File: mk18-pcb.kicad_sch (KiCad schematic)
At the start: 77 parts, among them J10 Conn_02x07_Top_Bottom, J17 Conn_01x06_Socket, J18 Conn_01x06_Socket, J19 Conn_01x06_Socket, J20 Conn_01x06_Socket, J7 Conn_02x06_Top_Bottom, J8 Conn_02x07_Top_Bottom, J9 Conn_02x06_Top_Bottom, P1 FH26W-13S-0_3SHW(60), P10 FH26W-13S-0_3SHW(60), P11 FH26W-13S-0_3SHW(60), P2 FH26W-13S-0_3SHW(60), P3 FH26W-13S-0_3SHW(60), P4 FH26W-13S-0_3SHW(60), P5 FH26W-13S-0_3SHW(60), P6 FH26W-13S-0_3SHW(60), P7 FH26W-13S-0_3SHW(60), P8 FH26W-13S-0_3SHW(60), P9 FH26W-13S-0_3SHW(60), U1 TYPE-C-31-M-12, U10 1N4148W_C81598, U11 1N4148W_C81598, U12 1N4148W_C81598, U13 1N4148W_C81598, U14 1N4148W_C81598, U15 1N4148W_C81598, U16 ECT818001569, U17 HC-FPC-05-10-16RLTAG, U2 AZC199-04S-MS, U4 SN74LVC1T45DRL, U9 1N4148W_C81598

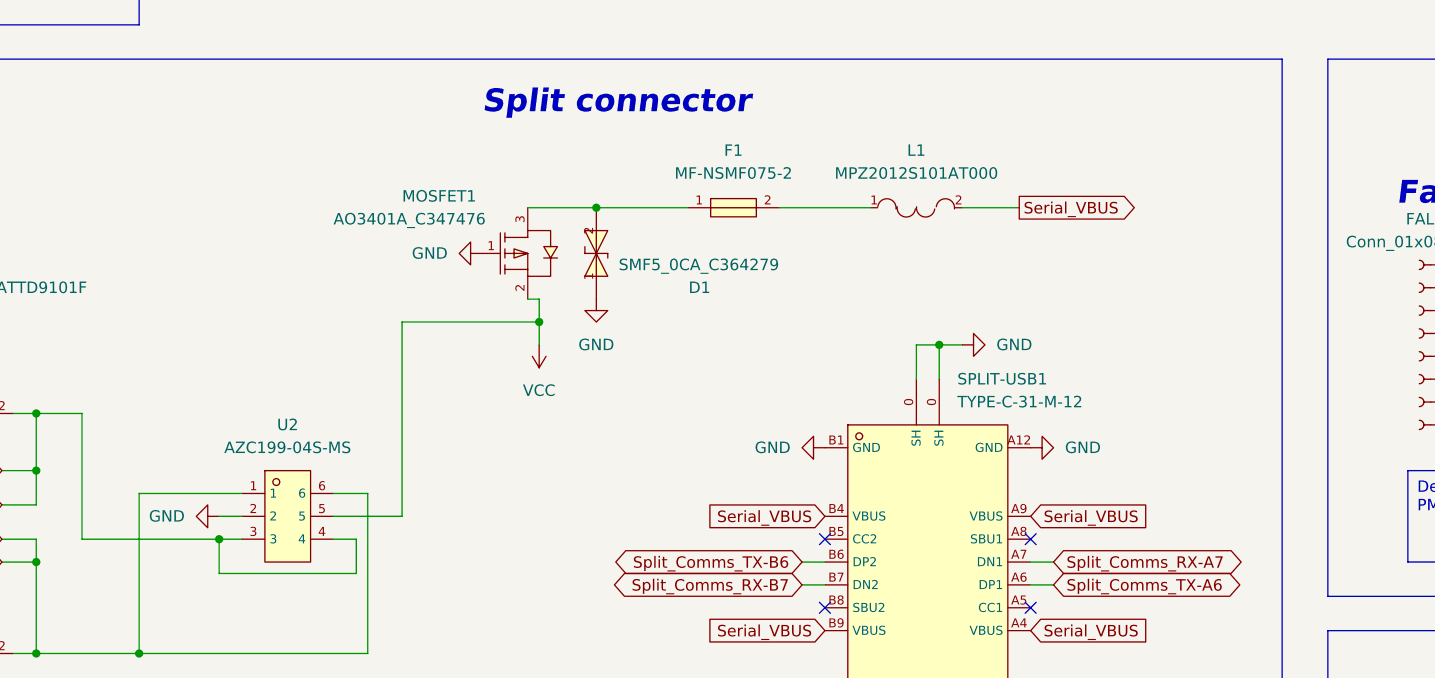
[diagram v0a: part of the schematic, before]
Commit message: added bypass for safeties
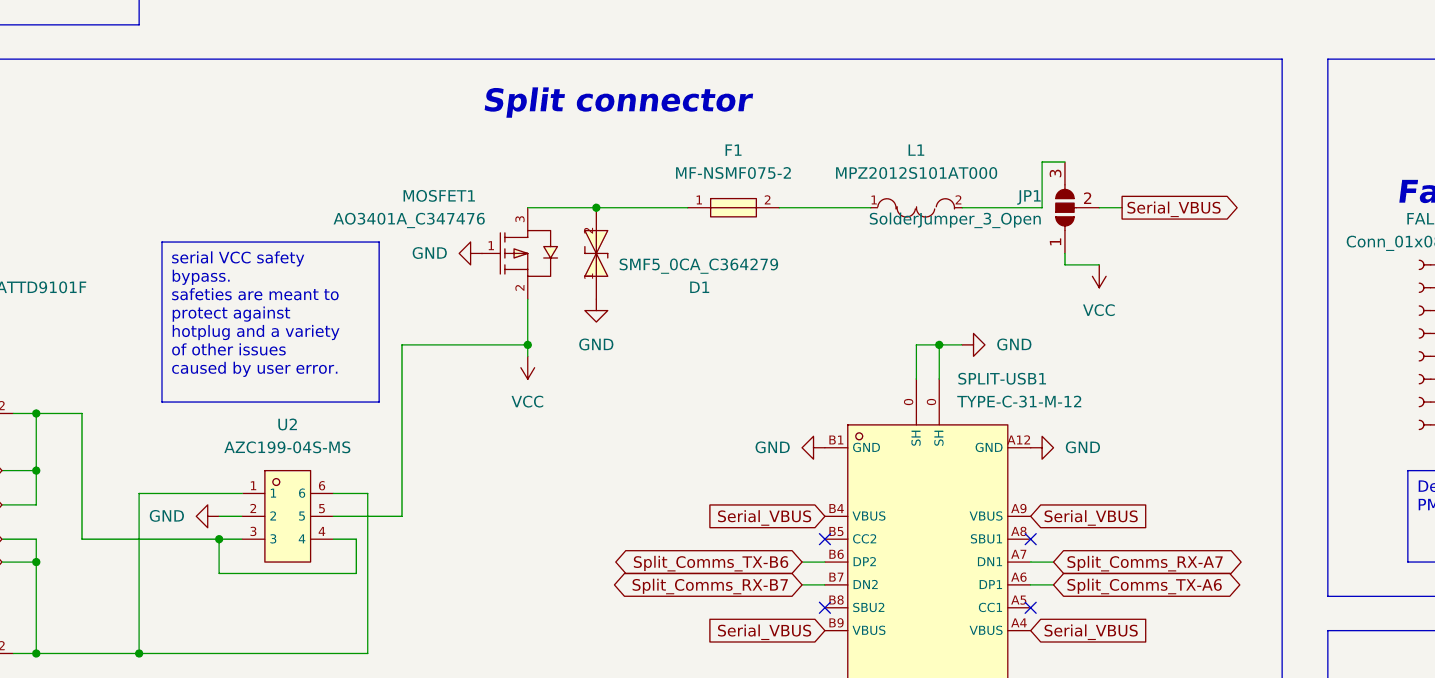
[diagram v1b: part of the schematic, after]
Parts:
- added JP1: SolderJumper_3_Open, Jumper:SolderJumper-3_P1.3mm_Open_RoundedPad1.0x1.5mm, symbol Jumper:SolderJumper_3_Open
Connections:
- net Serial_VBUS: now also JP1.2 (C); no longer L1.2
- net VCC: now also JP1.1 (A)
- new net: JP1.3 (B), L1.2
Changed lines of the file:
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@@
   (junction (at 361.95 284.48) (diameter 0) (color 0 0 0 0)
   )
-  (junction (at 111.76 92.71) (diameter 0) (color 0 0 0 0)
-  )
   (junction (at 232.41 149.86) (diameter 0) (color 0 0 0 0)
   )
@@
   (junction (at 67.31 129.54) (diameter 0) (color 0 0 0 0)
   )
+  (junction (at 110.49 95.25) (diameter 0) (color 0 0 0 0)
+  )
   (junction (at 400.05 185.42) (diameter 0) (color 0 0 0 0)
   )
@@
     (stroke (width 0) (type default))
   )
+  (wire (pts (xy 96.52 95.25) (xy 96.52 114.3))
+    (stroke (width 0) (type default))
+  )
   (wire (pts (xy 295.91 212.09) (xy 295.91 213.36))
     (stroke (width 0) (type default))
@@
     (stroke (width 0) (type default))
   )
-  (wire (pts (xy 111.76 92.71) (xy 111.76 95.25))
-    (stroke (width 0) (type default))
-  )
   (wire (pts (xy 276.86 203.2) (xy 279.4 203.2))
     (stroke (width 0) (type default))
@@
     (stroke (width 0) (type default))
   )
+  (wire (pts (xy 170.18 85.09) (xy 170.18 86.36))
+    (stroke (width 0) (type default))
+  )
   (wire (pts (xy 266.7 276.86) (xy 270.51 276.86))
     (stroke (width 0) (type default))
@@
     (stroke (width 0) (type default))
   )
-  (wire (pts (xy 110.49 90.17) (xy 111.76 90.17))
-    (stroke (width 0) (type default))
-  )
   (wire (pts (xy 214.63 93.98) (xy 224.79 93.98))
     (stroke (width 0) (type default))
@@
     (stroke (width 0) (type default))
   )
-  (wire (pts (xy 111.76 90.17) (xy 111.76 92.71))
-    (stroke (width 0) (type default))
-  )
   (wire (pts (xy 232.41 157.48) (xy 236.22 157.48))
     (stroke (width 0) (type default))
@@
     (stroke (width 0) (type default))
   )
-  (wire (pts (xy 158.75 80.01) (xy 165.1 80.01))
-    (stroke (width 0) (type default))
-  )
   (wire (pts (xy 610.87 280.67) (xy 610.87 292.1))
     (stroke (width 0) (type default))
@@
     (stroke (width 0) (type default))
   )
+  (wire (pts (xy 170.18 86.36) (xy 173.99 86.36))
+    (stroke (width 0) (type default))
+  )
   (wire (pts (xy 359.41 275.59) (xy 359.41 280.67))
     (stroke (width 0) (type default))
@@
     (stroke (width 0) (type default))
   )
+  (wire (pts (xy 173.99 80.01) (xy 176.53 80.01))
+    (stroke (width 0) (type default))
+  )
   (wire (pts (xy 459.74 254) (xy 457.2 254))
     (stroke (width 0) (type default))
@@
     (stroke (width 0) (type default))
   )
+  (wire (pts (xy 110.49 95.25) (xy 110.49 96.52))
+    (stroke (width 0) (type default))
+  )
   (wire (pts (xy 619.76 220.98) (xy 619.76 223.52))
     (stroke (width 0) (type default))
@@
     (stroke (width 0) (type default))
   )
+  (wire (pts (xy 96.52 95.25) (xy 110.49 95.25))
+    (stroke (width 0) (type default))
+  )
   (wire (pts (xy 312.42 379.73) (xy 321.31 379.73))
     (stroke (width 0) (type default))
@@
     (stroke (width 0) (type default))
   )
+  (wire (pts (xy 167.64 74.93) (xy 170.18 74.93))
+    (stroke (width 0) (type default))
+  )
   (wire (pts (xy 71.12 210.82) (xy 93.98 210.82))
     (stroke (width 0) (type default))
@@
     (stroke (width 0) (type default))
   )
+  (wire (pts (xy 167.64 80.01) (xy 167.64 74.93))
+    (stroke (width 0) (type default))
+  )
   (wire (pts (xy 38.1 391.16) (xy 40.64 391.16))
     (stroke (width 0) (type default))
@@
     (stroke (width 0) (type default))
   )
-  (wire (pts (xy 111.76 92.71) (xy 96.52 92.71))
-    (stroke (width 0) (type default))
-  )
   (wire (pts (xy 365.76 368.3) (xy 368.3 368.3))
     (stroke (width 0) (type default))
@@
     (stroke (width 0) (type default))
   )
-  (wire (pts (xy 96.52 92.71) (xy 96.52 114.3))
-    (stroke (width 0) (type default))
-  )
   (wire (pts (xy 401.32 217.17) (xy 403.86 217.17))
     (stroke (width 0) (type default))
@@
     (stroke (width 0) (type default))
   )
+  (wire (pts (xy 110.49 90.17) (xy 110.49 95.25))
+    (stroke (width 0) (type default))
+  )
   (wire (pts (xy 234.95 382.27) (xy 234.95 386.08))
     (stroke (width 0) (type default))
@@
     (stroke (width 0) (type default))
   )
+  (wire (pts (xy 158.75 80.01) (xy 167.64 80.01))
+    (stroke (width 0) (type default))
+  )
   (wire (pts (xy 492.76 403.86) (xy 495.3 403.86))
     (stroke (width 0) (type default))
@@
     (effects (font (size 1.27 1.27)) (justify left top))
   )
+  (text_box "serial VCC safety bypass.\nsafeties are meant to protect against hotplug and a variety of other issues caused by user error."
+    (at 69.85 83.82 0) (size 24.13 17.78)
+    (stroke (width 0) (type default))
+    (fill (type none))
+    (effects (font (size 1.27 1.27)) (justify left top))
+  )
   (text_box "Design note: \nThis connector needs to go on the siiiiide oh wait.\nRight in the middle.\n225mm center-of-mainpcb to connector.  \nShould be ok w. 30cm cable."
     (at 441.96 266.7 0) (size 35.56 17.78)
@@
     )
   )
-  (global_label "Serial_VBUS" (shape output) (at 165.1 80.01 0) (fields_autoplaced)
+  (global_label "Serial_VBUS" (shape output) (at 176.53 80.01 0) (fields_autoplaced)
     (effects (font (size 1.27 1.27)) (justify left))
-    (property "Intersheetrefs" "${INTERSHEET_REFS}" (at 179.4547 80.01 0)
+    (property "Intersheetrefs" "${INTERSHEET_REFS}" (at 190.8847 80.01 0)
       (effects (font (size 1.27 1.27)) (justify left) hide)
     )
@@
     )
   )
+  (symbol (lib_id "Jumper:SolderJumper_3_Open") (at 170.18 80.01 90) (unit 1)
+    (in_bom yes) (on_board yes) (dnp no) (fields_autoplaced)
+    (property "Reference" "JP1" (at 167.64 78.74 90)
+      (effects (font (size 1.27 1.27)) (justify left))
+    )
+    (property "Value" "SolderJumper_3_Open" (at 167.64 81.28 90)
+      (effects (font (size 1.27 1.27)) (justify left))
+    )
+    (property "Footprint" "Jumper:SolderJumper-3_P1.3mm_Open_RoundedPad1.0x1.5mm" (at 170.18 80.01 0)
+      (effects (font (size 1.27 1.27)) hide)
+    )
+    (property "Datasheet" "~" (at 170.18 80.01 0)
+      (effects (font (size 1.27 1.27)) hide)
+    )
+    (pin "1")
+    (pin "2")
+    (pin "3")
+    (instances
+      (project "mk18-pcb"
+        (path "/bb2be946-374e-4172-8486-a9a12db7ac7b"
+          (reference "JP1") (unit 1)
+        )
+      )
+    )
+  )
   (symbol (lib_id "power:GND") (at 414.02 217.17 90) (unit 1)
     (in_bom yes) (on_board yes) (dnp no) (fields_autoplaced)
@@
     )
   )
-  (symbol (lib_id "power:VCC") (at 111.76 95.25 180) (unit 1)
+  (symbol (lib_id "power:VCC") (at 110.49 96.52 180) (unit 1)
     (in_bom yes) (on_board yes) (dnp no) (fields_autoplaced)
-    (property "Reference" "#PWR0127" (at 111.76 91.44 0)
+    (property "Reference" "#PWR0127" (at 110.49 92.71 0)
       (effects (font (size 1.27 1.27)) hide)
     )
-    (property "Value" "VCC" (at 111.76 100.33 0)
+    (property "Value" "VCC" (at 110.49 101.6 0)
       (effects (font (size 1.27 1.27)))
     )
-    (property "Footprint" "" (at 111.76 95.25 0)
+    (property "Footprint" "" (at 110.49 96.52 0)
       (effects (font (size 1.27 1.27)) hide)
     )
-    (property "Datasheet" "" (at 111.76 95.25 0)
+    (property "Datasheet" "" (at 110.49 96.52 0)
       (effects (font (size 1.27 1.27)) hide)
     )
@@
         )
       )
+    )
+  )
+  (symbol (lib_id "power:VCC") (at 173.99 86.36 180) (unit 1)
+    (in_bom yes) (on_board yes) (dnp no) (fields_autoplaced)
+    (property "Reference" "#PWR069" (at 173.99 82.55 0)
+      (effects (font (size 1.27 1.27)) hide)
+    )
+    (property "Value" "VCC" (at 173.99 91.44 0)
+      (effects (font (size 1.27 1.27)))
+    )
+    (property "Footprint" "" (at 173.99 86.36 0)
+      (effects (font (size 1.27 1.27)) hide)
+    )
+    (property "Datasheet" "" (at 173.99 86.36 0)
+      (effects (font (size 1.27 1.27)) hide)
+    )
+    (pin "1")
+    (instances
+      (project "mk18-pcb"
+        (path "/bb2be946-374e-4172-8486-a9a12db7ac7b"
+          (reference "#PWR069") (unit 1)
+        )
+      )

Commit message: prior to removing pull-up resistors on comms
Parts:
- added GPIO1, LCD1: Conn_01x08_Socket, Connector_JST:JST_XH_B8B-XH-A_1x08_P2.50mm_Vertical, symbol Connector:Conn_01x08_Socket
- added HAND1: SolderJumper_3_Open, Jumper:SolderJumper-3_P1.3mm_Open_RoundedPad1.0x1.5mm, symbol Jumper:SolderJumper_3_Open
- added PWR-OUT1: Conn_01x03_Socket, Connector_JST:JST_EH_B3B-EH-A_1x03_P2.50mm_Vertical, symbol Connector:Conn_01x03_Socket
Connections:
- net +3V3: now also HAND1.3 (B), LCD1.2 (Pin_2), PWR-OUT1.2 (Pin_2)
- net GND: now also HAND1.1 (A), LCD1.1 (Pin_1), PWR-OUT1.1 (Pin_1)
- net SPI1_CLK: now also LCD1.5 (Pin_5)
- net SPI1_MOSI: now also LCD1.4 (Pin_4)
- net VCC: now also PWR-OUT1.3 (Pin_3)
- net GPIO7: now reaches PICO1.10 (GPIO7)
- net GPIO7: now also GPIO1.4 (Pin_4)
- net GPIO8: now reaches PICO1.11 (GPIO8)
- net GPIO8: now also GPIO1.5 (Pin_5)
- net LCD_DC: now reaches PICO1.19 (GPIO14)
- net LCD_DC: now also LCD1.7 (Pin_7)
- net LCD_BL: now reaches PICO1.20 (GPIO15)
- net LCD_BL: now also LCD1.8 (Pin_8)
- net LCD_CS: now reaches PICO1.21 (GPIO16)
- net LCD_CS: now also LCD1.3 (Pin_3)
- net LCD_RST: now reaches PICO1.22 (GPIO17)
- net LCD_RST: now also LCD1.6 (Pin_6)
- net GPIO22: now reaches PICO1.29 (GPIO22)
- net GPIO22: now also GPIO1.6 (Pin_6)
- net GPIO26: now reaches PICO1.31 (GPIO26_ADC0)
- net GPIO26: now also GPIO1.7 (Pin_7)
- net GPIO27: now reaches PICO1.32 (GPIO27_ADC1)
- net GPIO27: now also GPIO1.8 (Pin_8)
- net at PICO1.4 (GPIO2): now also HAND1.2 (C)
- net GPIO3: now reaches PICO1.5 (GPIO3)
- net GPIO3: now also GPIO1.1 (Pin_1)
- net GPIO4: now reaches PICO1.6 (GPIO4)
- net GPIO4: now also GPIO1.2 (Pin_2)
- net GPIO6: now reaches PICO1.9 (GPIO6)
- net GPIO6: now also GPIO1.3 (Pin_3)
- no-connect marks 42 -> 35
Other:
- note added: "GPIO"
- note added: "LCD"
- moved on the sheet: C5, C6, PICO1

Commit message: jan6 updates, added 5way, moved all vias off silkscreen, added breakouts
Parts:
- removed GPIO1: Conn_01x08_Socket, Connector_JST:JST_XH_B8B-XH-A_1x08_P2.50mm_Vertical, symbol Connector:Conn_01x08_Socket
- removed R1, R2: 120, ct-kicad:R0805, symbol kicad-symbols:WR08X1200FTL
- removed R3, R6: RK73H2ATTD9101F, ct-kicad:R0805, symbol kicad-symbols:RK73H2ATTD9101F
- removed R4, R5: WR08X1200FTL, ct-kicad:R0805, symbol kicad-symbols:WR08X1200FTL
- added 5WAY1: Conn_01x06_Socket, Connector_JST:JST_EH_B6B-EH-A_1x06_P2.50mm_Vertical, symbol Connector:Conn_01x06_Socket
- added ADC1: Conn_01x03_Socket, Connector_JST:JST_EH_B3B-EH-A_1x03_P2.50mm_Vertical, symbol Connector:Conn_01x03_Socket
- added G22, G3, G4, G6, G7, G8: Conn_01x01_Socket, Connector_Pin:Pin_D1.0mm_L10.0mm, symbol Connector:Conn_01x01_Socket
- added U3, U4, U5, U6, U7: 1N4148W_C81598, ct-kicad:SOD-123F_L2.7-W1.6-LS3.8-RD, symbol kicad-symbols:1N4148W_C81598
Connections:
- net Split_Comms_RX-A7 is gone; now on net Split_Comms_RX: SPLIT-USB1.A7 (DN1), SPLIT-USB1.B7 (DN2), U2.1, U2.6
- net Split_Comms_TX-A6 is gone; now on net Split_Comms_TX: SPLIT-USB1.A6 (DP1), SPLIT-USB1.B6 (DP2), U2.3, U2.4
- net GPIO22: now also G22.1 (Pin_1)
- net GPIO26: now also ADC1.2 (Pin_2)
- net GPIO27: now also ADC1.3 (Pin_3)
- net GPIO3: now also G3.1 (Pin_1)
- net GPIO4: now also G4.1 (Pin_1)
- net GPIO6: now also G6.1 (Pin_1)
- net GPIO7: now also G7.1 (Pin_1)
- net GPIO8: now also G8.1 (Pin_1)
- net col0: now also U3.1 (K)
- net col1: now also U5.1 (K)
- net col2: now also U6.1 (K)
- net col3: now also U7.1 (K)
- net col4: now also U4.1 (K)
- net row10: now also 5WAY1.5 (Pin_5)
- net AGND: now reaches PICO1.33 (AGND)
- net AGND: now also ADC1.1 (Pin_1)
- new net: 5WAY1.2 (Pin_2), U4.2 (A)
- new net: 5WAY1.1 (Pin_1), U3.2 (A)
- new net: 5WAY1.3 (Pin_3), U5.2 (A)
- new net: 5WAY1.4 (Pin_4), U6.2 (A)
- new net: 5WAY1.6 (Pin_6), U7.2 (A)
- no-connect marks 35 -> 34
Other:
- note added: "5-way"
- note added: "ADC breakout"
- note added: "GPIO breakout"
- note added: "Power breakout"
- note removed: "GPIO"
- moved on the sheet: PWR-OUT1

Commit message: really close now maybe kinda
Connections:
- net col0: now also FAL1.6 (Pin_6)
- net col1: now also FAL2.6 (Pin_6)
- net fal1-col: no longer FAL1.6 (Pin_6)
- net fal1-row: no longer FAL1.5 (Pin_5)
- net fal2-col: no longer FAL2.6 (Pin_6)
- net fal2-row: no longer FAL2.5 (Pin_5)
- net row11: now also FAL1.5 (Pin_5), FAL2.5 (Pin_5)
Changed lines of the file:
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@@
     )
   )
-  (global_label "fal1-row" (shape input) (at 224.79 93.98 0) (fields_autoplaced)
-    (effects (font (size 1.27 1.27)) (justify left))
-    (property "Intersheetrefs" "${INTERSHEET_REFS}" (at 236.3627 93.98 0)
+  (global_label "row11" (shape input) (at 224.79 93.98 0) (fields_autoplaced)
+    (effects (font (size 1.27 1.27)) (justify left))
+    (property "Intersheetrefs" "${INTERSHEET_REFS}" (at 233.4599 93.98 0)
       (effects (font (size 1.27 1.27)) (justify left) hide)
     )
@@
     )
   )
-  (global_label "fal1-col" (shape output) (at 224.79 91.44 0) (fields_autoplaced)
-    (effects (font (size 1.27 1.27)) (justify left))
-    (property "Intersheetrefs" "${INTERSHEET_REFS}" (at 235.9998 91.44 0)
+  (global_label "col0" (shape output) (at 224.79 91.44 0) (fields_autoplaced)
+    (effects (font (size 1.27 1.27)) (justify left))
+    (property "Intersheetrefs" "${INTERSHEET_REFS}" (at 231.8875 91.44 0)
       (effects (font (size 1.27 1.27)) (justify left) hide)
     )
@@
     )
   )
-  (global_label "fal2-row" (shape input) (at 264.16 93.98 0) (fields_autoplaced)
-    (effects (font (size 1.27 1.27)) (justify left))
-    (property "Intersheetrefs" "${INTERSHEET_REFS}" (at 275.7327 93.98 0)
+  (global_label "row11" (shape input) (at 264.16 93.98 0) (fields_autoplaced)
+    (effects (font (size 1.27 1.27)) (justify left))
+    (property "Intersheetrefs" "${INTERSHEET_REFS}" (at 272.8299 93.98 0)
       (effects (font (size 1.27 1.27)) (justify left) hide)
     )
@@
     )
   )
-  (global_label "fal2-col" (shape output) (at 264.16 91.44 0) (fields_autoplaced)
-    (effects (font (size 1.27 1.27)) (justify left))
-    (property "Intersheetrefs" "${INTERSHEET_REFS}" (at 275.3698 91.44 0)
-      (effects (font (size 1.27 1.27)) (justify left) hide)
-    )
+  (global_label "col1" (shape output) (at 264.16 91.44 0) (fields_autoplaced)
+    (effects (font (size 1.27 1.27)) (justify left))
+    (property "Intersheetrefs" "${INTERSHEET_REFS}" (at 271.2575 91.44 0)
+      (effects (font (size 1.27 1.27)) (justify left) hide)
+    )

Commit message: added debug, test points, more
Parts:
- added DBG1: Conn_01x03_Socket, Connector_JST:JST_EH_B3B-EH-A_1x03_P2.50mm_Vertical, symbol Connector:Conn_01x03_Socket
- added T1, T10, T2, T3, T4, T5, T6, T7, T8, T9: Conn_01x01_Socket, Connector_Pin:Pin_D1.0mm_L10.0mm, symbol Connector:Conn_01x01_Socket
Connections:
- net COL_CS: now also T5.1 (Pin_1)
- net COL_CS_MOS: now also T10.1 (Pin_1)
- net LED_DI_3.3V: now also T8.1 (Pin_1)
- net LED_KEYS_DI: now also T9.1 (Pin_1)
- net ROW_CS: now also T4.1 (Pin_1)
- net SPI1_CLK: now also T1.1 (Pin_1)
- net SPI1_MISO: now also T3.1 (Pin_1)
- net SPI1_MOSI: now also T2.1 (Pin_1)
- net Split_Comms_RX: now also T7.1 (Pin_1)
- net Split_Comms_TX: now also T6.1 (Pin_1)
- net SWCLK: now reaches PICO1.41 (SWCLK)
- net SWCLK: now also DBG1.3 (Pin_3)
- net SWGND: now reaches PICO1.42 (GND)
- net SWGND: now also DBG1.2 (Pin_2)
- net SWDIO: now reaches PICO1.43 (SWDIO)
- net SWDIO: now also DBG1.1 (Pin_1)
- no-connect marks 34 -> 31
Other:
- note added: "Debug breakout"
- note added: "Test points"

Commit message: before updating the macropad connector
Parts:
- removed H5: MountingHole, MountingHole:MountingHole_3.2mm_M3, symbol Mechanical:MountingHole
- H1, H2, H3, H4: footprint MountingHole:MountingHole_3.2mm_M3 -> MountingHole:MountingHole_3.2mm_M3_Pad_Via
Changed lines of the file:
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@@
     )
   )
-  (symbol (lib_id "Mechanical:MountingHole") (at 29.21 54.61 0) (unit 1)
-    (in_bom yes) (on_board yes) (dnp no) (fields_autoplaced)
-    (property "Reference" "H5" (at 31.75 53.34 0)
-      (effects (font (size 1.27 1.27)) (justify left))
-    )
-    (property "Value" "MountingHole" (at 31.75 55.88 0)
-      (effects (font (size 1.27 1.27)) (justify left))
-    )
-    (property "Footprint" "MountingHole:MountingHole_3.2mm_M3" (at 29.21 54.61 0)
-      (effects (font (size 1.27 1.27)) hide)
-    )
-    (property "Datasheet" "~" (at 29.21 54.61 0)
-      (effects (font (size 1.27 1.27)) hide)
-    )
-    (instances
-      (project "mk18-pcb"
-        (path "/bb2be946-374e-4172-8486-a9a12db7ac7b"
-          (reference "H5") (unit 1)
-        )
-      )
-    )
-  )
   (symbol (lib_id "power:GND") (at 152.4 400.05 0) (unit 1)
     (in_bom yes) (on_board yes) (dnp no) (fields_autoplaced)
@@
       (effects (font (size 1.27 1.27)) (justify left))
     )
-    (property "Footprint" "MountingHole:MountingHole_3.2mm_M3" (at 29.21 41.91 0)
+    (property "Footprint" "MountingHole:MountingHole_3.2mm_M3_Pad_Via" (at 29.21 41.91 0)
       (effects (font (size 1.27 1.27)) hide)
     )
@@
       (effects (font (size 1.27 1.27)) (justify left))
     )
-    (property "Footprint" "MountingHole:MountingHole_3.2mm_M3" (at 29.21 29.21 0)
+    (property "Footprint" "MountingHole:MountingHole_3.2mm_M3_Pad_Via" (at 29.21 29.21 0)
       (effects (font (size 1.27 1.27)) hide)
     )
@@
       (effects (font (size 1.27 1.27)) (justify left))
     )
-    (property "Footprint" "MountingHole:MountingHole_3.2mm_M3" (at 29.21 35.56 0)
+    (property "Footprint" "MountingHole:MountingHole_3.2mm_M3_Pad_Via" (at 29.21 35.56 0)
       (effects (font (size 1.27 1.27)) hide)
     )
@@
       (effects (font (size 1.27 1.27)) (justify left))
     )
-    (property "Footprint" "MountingHole:MountingHole_3.2mm_M3" (at 29.21 48.26 0)
+    (property "Footprint" "MountingHole:MountingHole_3.2mm_M3_Pad_Via" (at 29.21 48.26 0)
       (effects (font (size 1.27 1.27)) hide)
     )
